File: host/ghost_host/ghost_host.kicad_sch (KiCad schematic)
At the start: 1 part

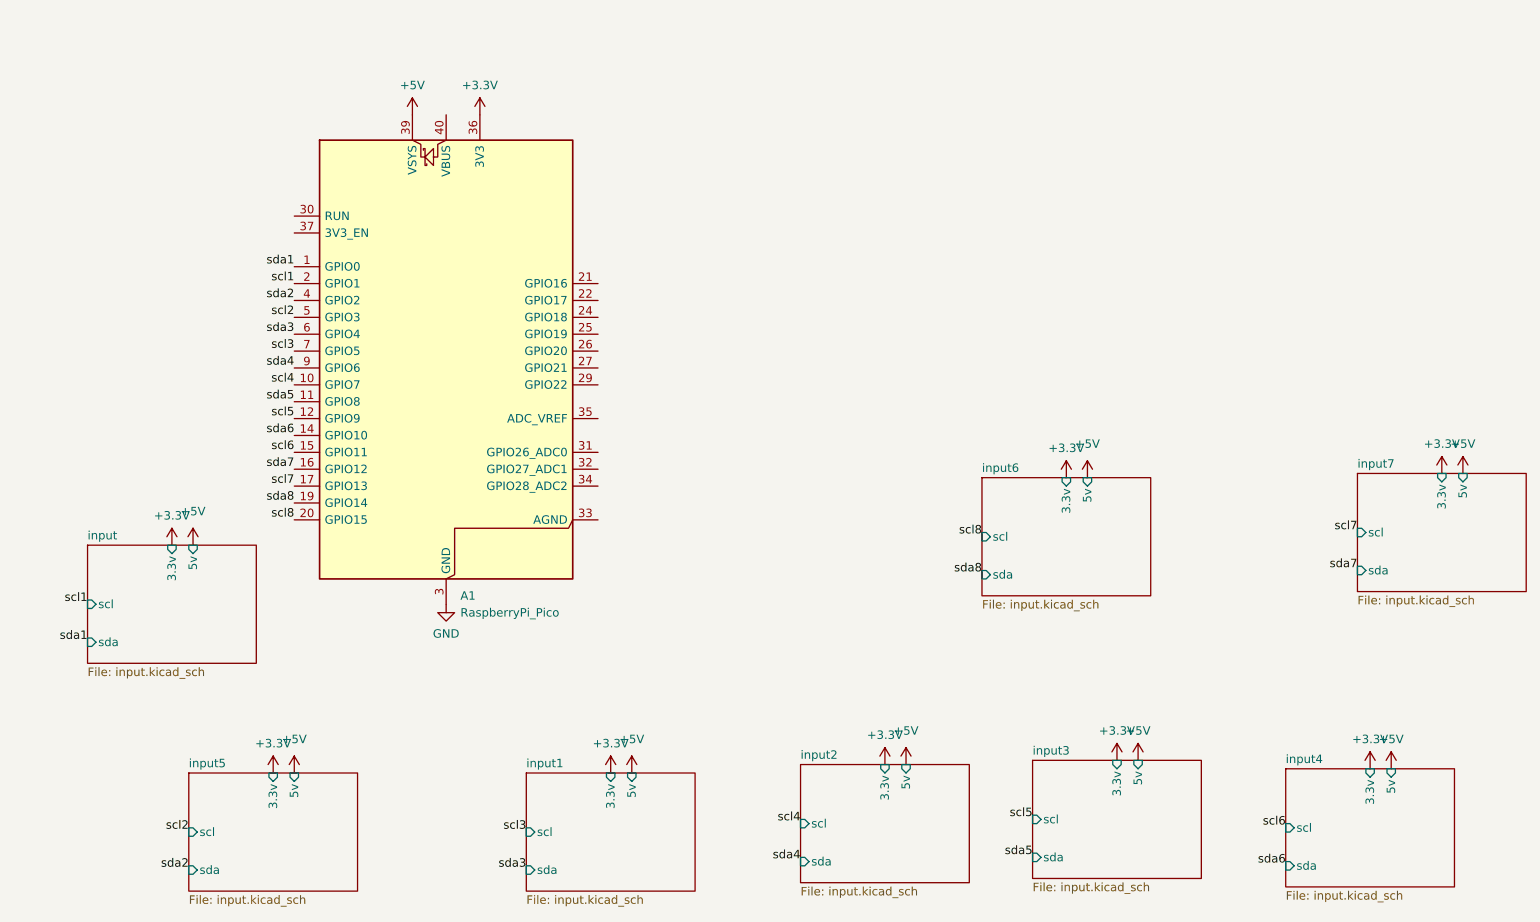
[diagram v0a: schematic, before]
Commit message: switched out raspPi pico to kb2040, added RGB connector, assigned footprints, created RJ12 footprint
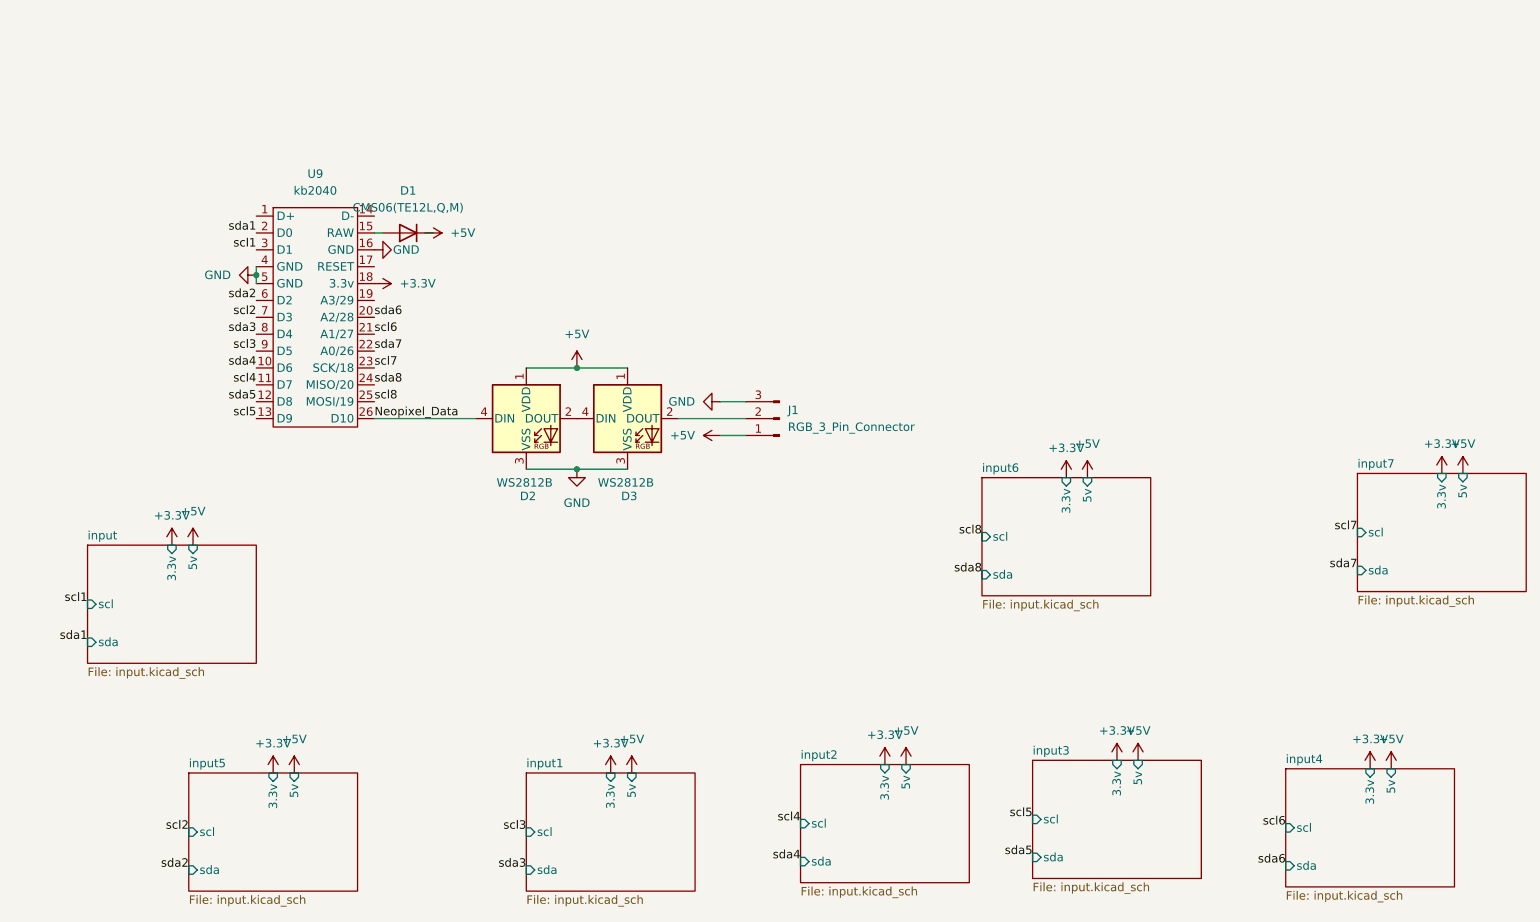
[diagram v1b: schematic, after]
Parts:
- removed A1: RaspberryPi_Pico, Module:RaspberryPi_Pico_Common_SMD, symbol MCU_Module:RaspberryPi_Pico
- added D1: CMS06(TE12L,Q,M), Diode_SMD:D_SOD-323_HandSoldering, symbol Device:D
- added D2, D3: WS2812B, LED_SMD:LED_WS2812B_PLCC4_5.0x5.0mm_P3.2mm, symbol LED:WS2812B
- added J1: RGB_3_Pin_Connector, Connector_PinHeader_2.54mm:PinHeader_1x03_P2.54mm_Horizontal, symbol Connector:Conn_01x03_Pin
- added U9: kb2040, kb2040:kb2040, symbol kb2040:kb2040
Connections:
- net +3.3V: now also U9.18 (3.3v)
- net +5V: now also D1.1 (K), D2.1 (VDD), D3.1 (VDD), J1.1 (Pin_1)
- net GND: now also D2.3 (VSS), D3.3 (VSS), J1.3 (Pin_3), U9.16 (GND), U9.4 (GND), U9.5 (GND)
- net scl1: now also U9.3 (D1)
- net scl2: now also U9.7 (D3)
- net scl3: now also U9.9 (D5)
- net scl4: now also U9.11 (D7)
- net scl5: now also U9.13 (D9)
- net scl6: now also U9.21 (A1/27)
- net scl7: now also U9.23 (SCK/18)
- net scl8: now also U9.25 (MOSI/19)
- net sda1: now also U9.2 (D0)
- net sda2: now also U9.6 (D2)
- net sda3: now also U9.8 (D4)
- net sda4: now also U9.10 (D6)
- net sda5: now also U9.12 (D8)
- net sda6: now also U9.20 (A2/28)
- net sda7: now also U9.22 (A0/26)
- net sda8: now also U9.24 (MISO/20)
- new net: D1.2 (A), U9.15 (RAW)
- new net: D2.2 (DOUT), D3.4 (DIN)
- new net: D3.2 (DOUT), J1.2 (Pin_2)
- new net Neopixel_Data: D2.4 (DIN), U9.26 (D10)

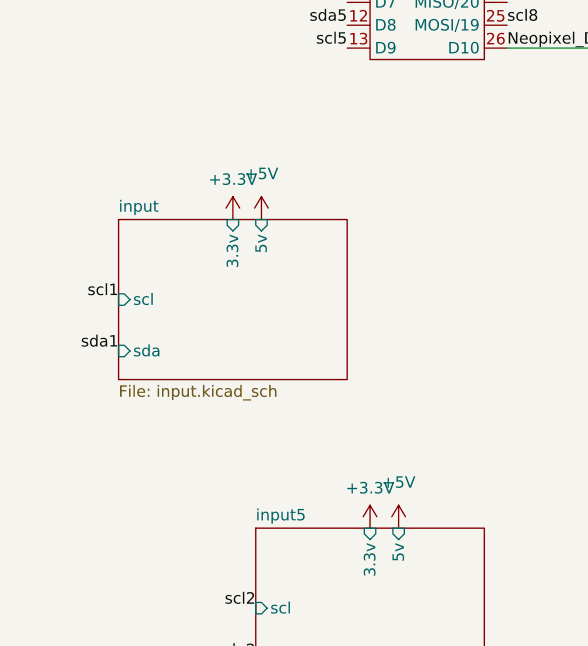
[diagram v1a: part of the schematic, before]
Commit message: updated resistor footprints, began prb layout
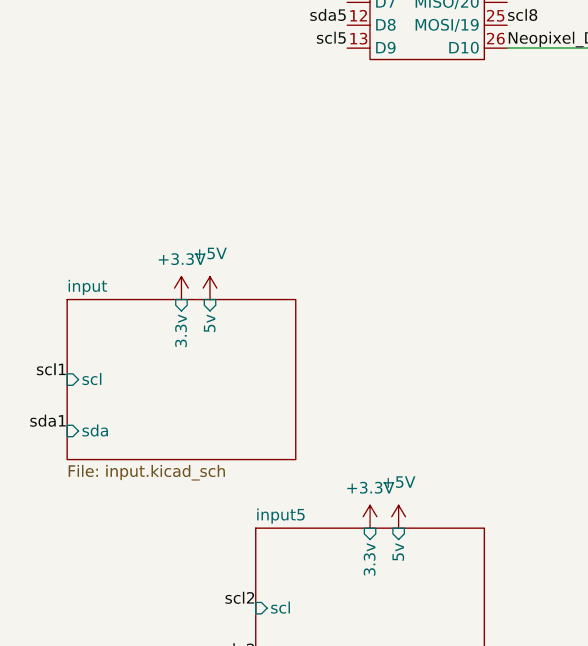
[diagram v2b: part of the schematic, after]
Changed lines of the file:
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@@
 	)
 	(label "scl1"
-		(at 43.18 107.95 180)
+		(at 37.465 116.84 180)
 		(effects
 			(font
@@
 	)
 	(label "sda1"
-		(at 43.18 113.665 180)
+		(at 37.465 122.555 180)
 		(effects
 			(font
@@
 	(symbol
 		(lib_id "power:+3.3V")
-		(at 55.88 99.06 0)
+		(at 50.165 107.95 0)
 		(unit 1)
 		(exclude_from_sim no)
@@
 		(fields_autoplaced yes)
 		(property "Reference" "#PWR034"
-			(at 55.88 102.87 0)
+			(at 50.165 111.76 0)
 			(effects
 				(font
@@
 		)
 		(property "Value" "+3.3V"
-			(at 55.88 94.615 0)
+			(at 50.165 103.505 0)
 			(effects
 				(font
@@
 		)
 		(property "Footprint" ""
-			(at 55.88 99.06 0)
+			(at 50.165 107.95 0)
 			(effects
 				(font
@@
 		)
 		(property "Datasheet" ""
-			(at 55.88 99.06 0)
+			(at 50.165 107.95 0)
 			(effects
 				(font
@@
 		)
 		(property "Description" "Power symbol creates a global label with name \"+3.3V\""
-			(at 55.88 99.06 0)
+			(at 50.165 107.95 0)
 			(effects
 				(font
@@
 	(symbol
 		(lib_id "power:+5V")
-		(at 59.055 99.06 0)
+		(at 53.34 107.95 0)
 		(unit 1)
 		(exclude_from_sim no)
@@
 		(fields_autoplaced yes)
 		(property "Reference" "#PWR026"
-			(at 59.055 102.87 0)
+			(at 53.34 111.76 0)
 			(effects
 				(font
@@
 		)
 		(property "Value" "+5V"
-			(at 59.055 93.98 0)
+			(at 53.34 102.87 0)
 			(effects
 				(font
@@
 		)
 		(property "Footprint" ""
-			(at 59.055 99.06 0)
+			(at 53.34 107.95 0)
 			(effects
 				(font
@@
 		)
 		(property "Datasheet" ""
-			(at 59.055 99.06 0)
+			(at 53.34 107.95 0)
 			(effects
 				(font
@@
 		)
 		(property "Description" "Power symbol creates a global label with name \"+5V\""
-			(at 59.055 99.06 0)
+			(at 53.34 107.95 0)
 			(effects
 				(font
@@
 	)
 	(sheet
-		(at 43.18 99.06)
+		(at 37.465 107.95)
 		(size 25.4 17.78)
 		(exclude_from_sim no)
@@
 		)
 		(property "Sheetname" "input"
-			(at 43.18 98.3484 0)
+			(at 37.465 107.2384 0)
 			(effects
 				(font
@@
 		)
 		(property "Sheetfile" "input.kicad_sch"
-			(at 43.18 117.4246 0)
+			(at 37.465 126.3146 0)
 			(effects
 				(font
@@
 		)
 		(pin "scl" input
-			(at 43.18 107.95 180)
+			(at 37.465 116.84 180)
 			(effects
 				(font
@@
 		)
 		(pin "3.3v" input
-			(at 55.88 99.06 90)
+			(at 50.165 107.95 90)
 			(effects
 				(font
@@
 		)
 		(pin "sda" input
-			(at 43.18 113.665 180)
+			(at 37.465 122.555 180)
 			(effects
 				(font
@@
 		)
 		(pin "5v" input
-			(at 59.055 99.06 90)
-			(effects
-				(font
+			(at 53.34 107.95 90)
+			(effects
+				(font

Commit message: reorg pcb layout
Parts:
- added H1, H2, H3, H4: MountingHole_Pad, MountingHole:MountingHole_4.5mm_Pad_Via, symbol Mechanical:MountingHole_Pad
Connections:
- net GND: now also H1.1, H2.1, H3.1, H4.1

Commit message: make things nicerg
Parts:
- added H5, H6: MountingHole_Pad, MountingHole:MountingHole_4.5mm_Pad_Via, symbol Mechanical:MountingHole_Pad
- J1: now not fitted
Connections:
- net GND: now also H5.1, H6.1
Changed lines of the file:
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@@
 	(paper "A4")
+	(junction
+		(at 153.67 25.4)
+		(diameter 0)
+		(color 0 0 0 0)
+	)
 	(junction
 		(at 146.05 25.4)
@@
 	)
 	(junction
+		(at 161.29 25.4)
+		(diameter 0)
+		(color 0 0 0 0)
+	)
+	(junction
 		(at 116.84 87.63)
 		(diameter 0)
@@
 	(wire
 		(pts
-			(xy 137.16 25.4) (xy 142.24 25.4)
+			(xy 153.67 25.4) (xy 161.29 25.4)
 		)
 		(stroke
@@
 	(wire
 		(pts
-			(xy 129.54 25.4) (xy 137.16 25.4)
+			(xy 137.16 25.4) (xy 142.24 25.4)
 		)
 		(stroke
@@
 	(wire
 		(pts
-			(xy 142.24 82.55) (xy 138.43 82.55)
+			(xy 161.29 25.4) (xy 168.91 25.4)
 		)
 		(stroke
@@
 	(wire
 		(pts
-			(xy 68.58 58.42) (xy 68.58 59.69)
+			(xy 129.54 25.4) (xy 137.16 25.4)
 		)
 		(stroke
@@
 		)
 	)
+	(wire
+		(pts
+			(xy 142.24 82.55) (xy 138.43 82.55)
+		)
+		(stroke
+			(width 0)
+			(type default)
+		)
+	)
+	(wire
+		(pts
+			(xy 68.58 58.42) (xy 68.58 59.69)
+		)
+		(stroke
+			(width 0)
+			(type default)
+		)
+	)
 	(label "scl8"
 		(at 177.8 97.79 180)
@@
 	)
 	(symbol
+		(lib_id "Mechanical:MountingHole_Pad")
+		(at 168.91 22.86 0)
+		(unit 1)
+		(exclude_from_sim no)
+		(in_bom no)
+		(on_board yes)
+		(dnp no)
+		(fields_autoplaced yes)
+		(property "Reference" "H6"
+			(at 171.45 20.3199 0)
+			(effects
+				(font
+					(size 1.27 1.27)
+				)
+				(justify left)
+			)
+		)
+		(property "Value" "MountingHole_Pad"
+			(at 171.45 22.8599 0)
+			(effects
+				(font
+					(size 1.27 1.27)
+				)
+				(justify left)
+				(hide yes)
+			)
+		)
+		(property "Footprint" "MountingHole:MountingHole_4.5mm_Pad_Via"
+			(at 168.91 22.86 0)
+			(effects
+				(font
+					(size 1.27 1.27)
+				)
+				(hide yes)
+			)
+		)
+		(property "Datasheet" "~"
+			(at 168.91 22.86 0)
+			(effects
+				(font
+					(size 1.27 1.27)
+				)
+				(hide yes)
+			)
+		)
+		(property "Description" "Mounting Hole with connection"
+			(at 168.91 22.86 0)
+			(effects
+				(font
+					(size 1.27 1.27)
+				)
+				(hide yes)
+			)
+		)
+		(pin "1"
+		)
+		(instances
+			(project "ghost_host"
+				(path "/d931a957-36f8-4ac4-bfa7-9b0a51712375"
+					(reference "H6")
+					(unit 1)
+				)
+			)
+		)
+	)
+	(symbol
 		(lib_id "power:+3.3V")
 		(at 198.12 131.445 0)
@@
 		(in_bom yes)
 		(on_board yes)
-		(dnp no)
+		(dnp yes)
 		(fields_autoplaced yes)
 		(property "Reference" "J1"
@@
 					(unit 1)
 				)
+			)
+		)
+	)
+	(symbol
+		(lib_id "Mechanical:MountingHole_Pad")
+		(at 161.29 22.86 0)
+		(unit 1)
+		(exclude_from_sim no)
+		(in_bom no)
+		(on_board yes)
+		(dnp no)
+		(fields_autoplaced yes)
+		(property "Reference" "H5"
+			(at 163.83 20.3199 0)
+			(effects
+				(font
+					(size 1.27 1.27)
+				)
+				(justify left)
+			)
+		)
+		(property "Value" "MountingHole_Pad"
+			(at 163.83 22.8599 0)
+			(effects
+				(font
+					(size 1.27 1.27)
+				)
+				(justify left)
+				(hide yes)
+			)
+		)
+		(property "Footprint" "MountingHole:MountingHole_4.5mm_Pad_Via"
+			(at 161.29 22.86 0)
+			(effects
+				(font
+					(size 1.27 1.27)
+				)
+				(hide yes)
+			)
+		)
+		(property "Datasheet" "~"
+			(at 161.29 22.86 0)
+			(effects
+				(font
+					(size 1.27 1.27)
+				)
+				(hide yes)
+			)
+		)
+		(property "Description" "Mounting Hole with connection"
+			(at 161.29 22.86 0)
+			(effects
+				(font
+					(size 1.27 1.27)
+				)
+				(hide yes)
+			)
+		)
+		(pin "1"
+		)
+		(instances
+			(project "ghost_host"
+				(path "/d931a957-36f8-4ac4-bfa7-9b0a51712375"
+					(reference "H5")
+					(unit 1)
+				)

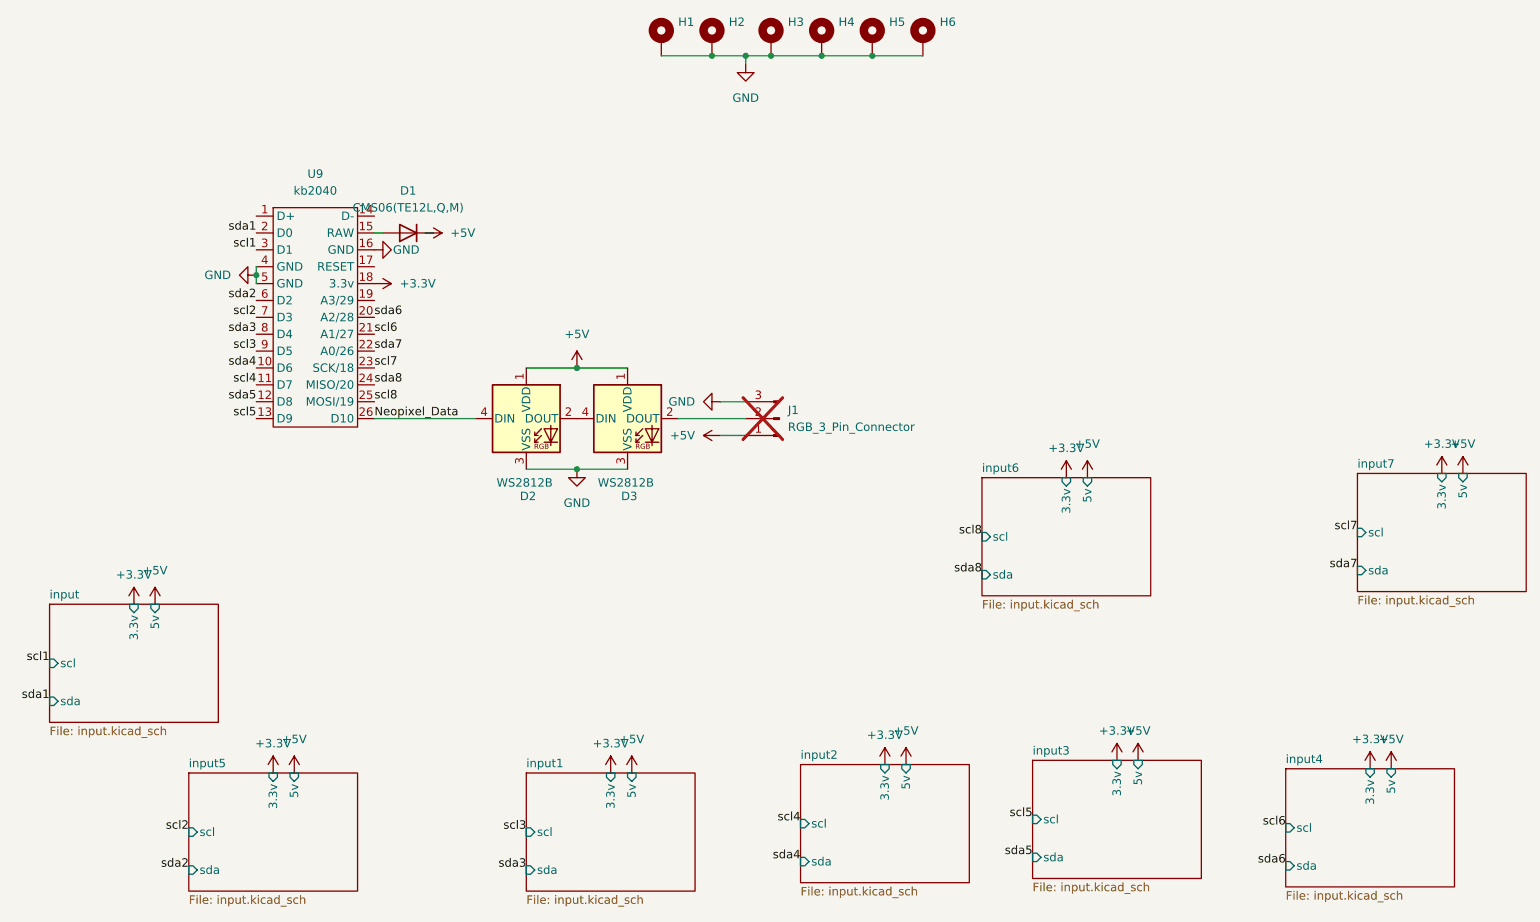
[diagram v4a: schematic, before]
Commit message: pcb review, added 3d models
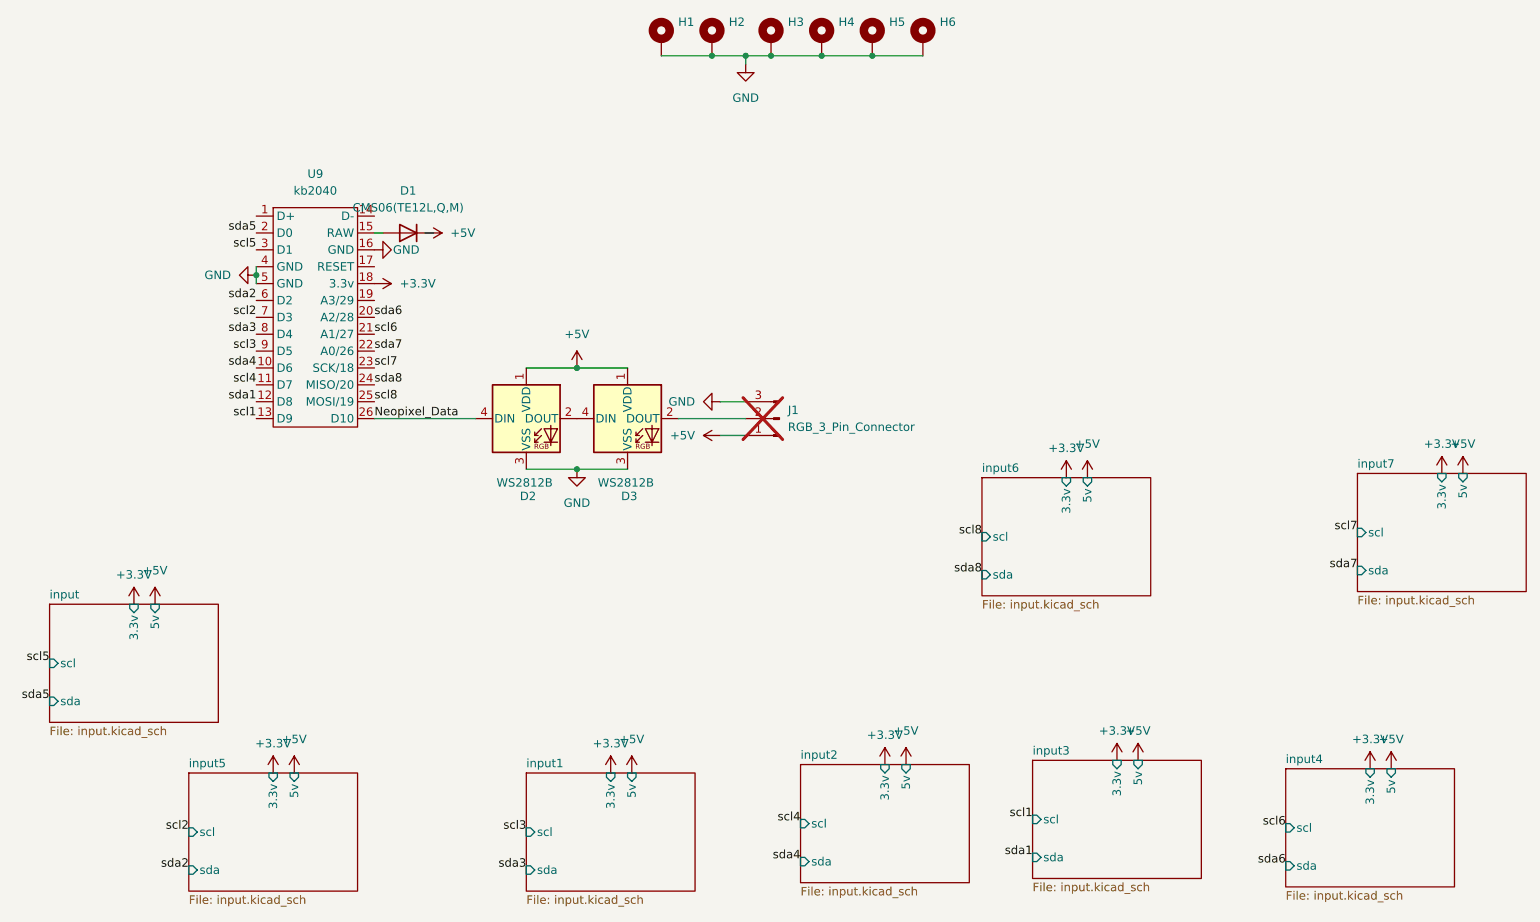
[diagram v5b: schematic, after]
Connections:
- net scl1: now also U9.13 (D9); no longer U9.3 (D1)
- net scl5: now also U9.3 (D1); no longer U9.13 (D9)
- net sda1: now also U9.12 (D8); no longer U9.2 (D0)
- net sda5: now also U9.2 (D0); no longer U9.12 (D8)
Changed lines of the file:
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@@
 		)
 	)
-	(label "sda1"
+	(label "sda5"
 		(at 68.58 52.07 180)
 		(effects
@@
 		)
 	)
-	(label "scl5"
+	(label "scl1"
 		(at 185.42 140.335 180)
 		(effects
@@
 		)
 	)
-	(label "scl1"
+	(label "scl5"
 		(at 68.58 54.61 180)
 		(effects
@@
 		)
 	)
-	(label "scl1"
+	(label "scl5"
 		(at 37.465 116.84 180)
 		(effects
@@
 		)
 	)
-	(label "sda5"
+	(label "sda1"
 		(at 185.42 146.05 180)
 		(effects
@@
 		)
 	)
-	(label "sda5"
+	(label "sda1"
 		(at 68.58 77.47 180)
 		(effects
@@
 		)
 	)
-	(label "scl5"
+	(label "scl1"
 		(at 68.58 80.01 180)
 		(effects
@@
 		)
 	)
-	(label "sda1"
+	(label "sda5"
 		(at 37.465 122.555 180)
 		(effects

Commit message: host w/ bom
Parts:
- D1: Manufacturer (none) -> Toshiba; Manufacturer Part Number (none) -> CMS06(TE12L,Q,M); Supplier Name (none) -> LCSC; Supplier Part Number (none) -> C261920
- D2, D3: Manufacturer (none) -> XINGLIGHT; Manufacturer Part Number (none) -> XL-5050RGBC-2812B; Supplier Name (none) -> LCSC; Supplier Part Number (none) -> C2843785
- U9: Manufacturer (none) -> Adafruit; Manufacturer Part Number (none) -> 5302; Supplier Name (none) -> Mouser/Digikey
